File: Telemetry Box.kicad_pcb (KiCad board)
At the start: 4 copper layers, 44.6 x 36.8 mm, 82 parts, among them J1 USB_C_Receptacle, J2 DC 5V In, J3 Conn_01x06, J4 Thermistor Molex, J5 Micro_SD_Card, J6 Thermistor Molex, J8 SMA, Q1 MMBT2222A-TP, SW2 SW_Push, U1 AP2112K-1.8, U10 MAX-M10S, U2 TPS62160DSG, U3 STM32F373CCTx, U4 LSM6DSRXTR, U5 MCP6L01x-xLT, U7 BMP585, U8 MCP6L01x-xLT, U9 USBLC6-2P6, X1 32.768kHz

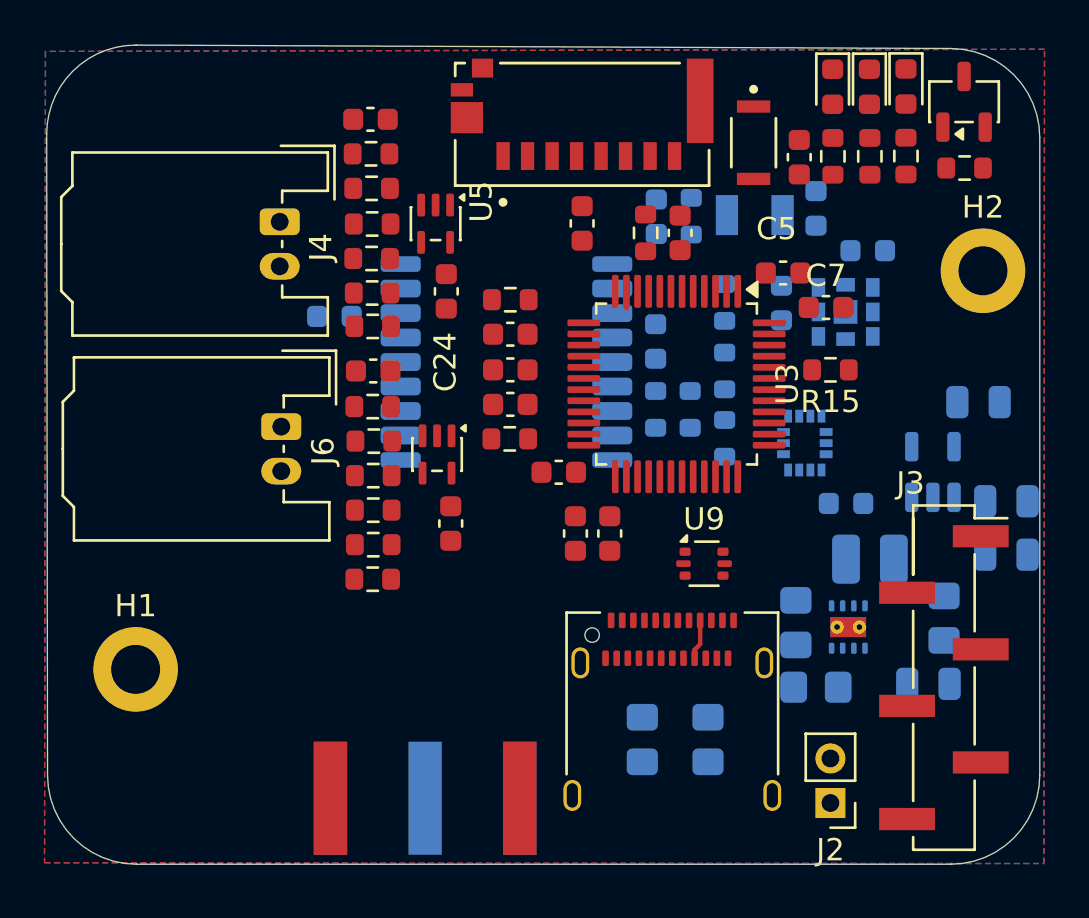
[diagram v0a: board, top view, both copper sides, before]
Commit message: Shrank board, updated all cap footprints. Updated thermistor headers to be vertical
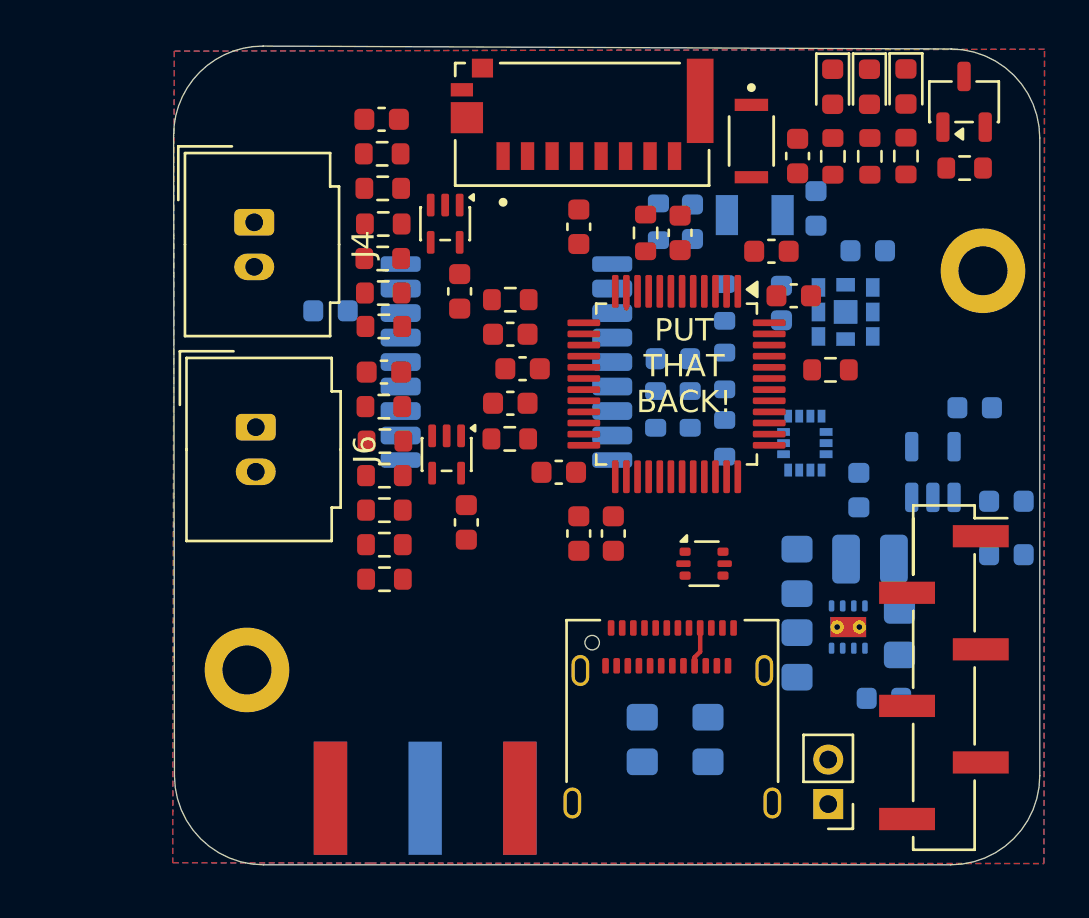
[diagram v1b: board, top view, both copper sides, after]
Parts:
- removed C11, C12, C17, C18, C20, C21, C5, C7, C9: 100nF, Capacitor_SMD:C_0603_1608Metric
- added C23: 100nF, Capacitor_SMD:C_0603_1608Metric, F.Cu at (131.7, 119.2)
- added C25: 100nF, Capacitor_SMD:C_0603_1608Metric, F.Cu at (128.3, 122.8)
- added C29: 100nF, Capacitor_SMD:C_0603_1608Metric, B.Cu at (125.9, 120.1)
- added C31: 100nF, Capacitor_SMD:C_0603_1608Metric, F.Cu at (134.0, 121.2)
- added C34: 100nF, Capacitor_SMD:C_0603_1608Metric, F.Cu at (146.7, 119.4)
- added C35: 100nF, Capacitor_SMD:C_0603_1608Metric, F.Cu at (138.6, 130.1)
- added C36: 100nF, Capacitor_SMD:C_0603_1608Metric, F.Cu at (145.7, 117.4)
- added C37: 100nF, Capacitor_SMD:C_0603_1608Metric, F.Cu at (134.5, 122.7)
- added C38: 100nF, Capacitor_SMD:C_0603_1608Metric, F.Cu at (137.1, 116.3)
- C1, C2: value 1u -> 1uF; footprint Capacitor_SMD:C_0805_2012Metric -> Capacitor_SMD:C_0603_1608Metric
- C28, C30: moved to B.Cu
- C3: value 10u -> 10uF; footprint Capacitor_SMD:C_0805_2012Metric -> Capacitor_SMD:C_0603_1608Metric
- C32, C33: moved to F.Cu
- C4: value 22u -> 22uF; footprint Capacitor_SMD:C_0805_2012Metric -> Capacitor_SMD:C_0603_1608Metric
- J4, J6: footprint Connector_Molex:Molex_MicroClasp_55935-0230_1x02_P2.00mm_Horizontal -> Connector_Molex:Molex_MicroClasp_55932-0230_1x02_P2.00mm_Vertical
- moved C33 22.0 mm to (146.9, 113.2), turned to -90 degrees
- moved C30 18.4 mm to (149.6, 128.2)
- moved C28 13.5 mm to (141.3, 122.2), turned to 0 degrees
- moved C24 10.4 mm to (132.0, 129.6)
- moved C32 7.09 mm to (134.0, 124.2), turned to 180 degrees
- moved H1 5.00 mm to (122.2, 136.2)
- moved R4 2.30 mm to (146.8, 131.8)
- moved C3 2.10 mm to (150.8, 137.5)
- moved R3 2.10 mm to (151.4, 134.6)
- moved R5 1.68 mm to (146.8, 135.6), turned to -90 degrees
- moved C16 1.64 mm to (142.2, 116.1)
- moved R9 1.50 mm to (140.6, 116.1)
- moved J4 1.15 mm to (122.5, 116.1)
- moved J6 1.15 mm to (122.5, 125.3)
- moved R31 0.53 mm to (128.3, 132.2)
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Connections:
- C28 pad 1: /MCU/THERM2 -> +3V3
- C30 pad 1: +3V3 -> +1V8
- C32 pad 1: +3V3 -> /MCU/THERM2_ADC
- C33 pad 1: +3V3 -> PGND
- C33 pad 2: PGND -> /MCU/RESET
- J4 pad 1: PGND -> /Sensors/THERM1_V-
- J4 pad 2: /Sensors/THERM1_V- -> PGND
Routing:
- added copper zone on In2.Cu, net +3V3
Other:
- board size 44.6 x 36.8 mm -> 38.9 x 36.8 mm
- board text added: "PUT THAT BACK!"

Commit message: Finished Rev2 signal routing
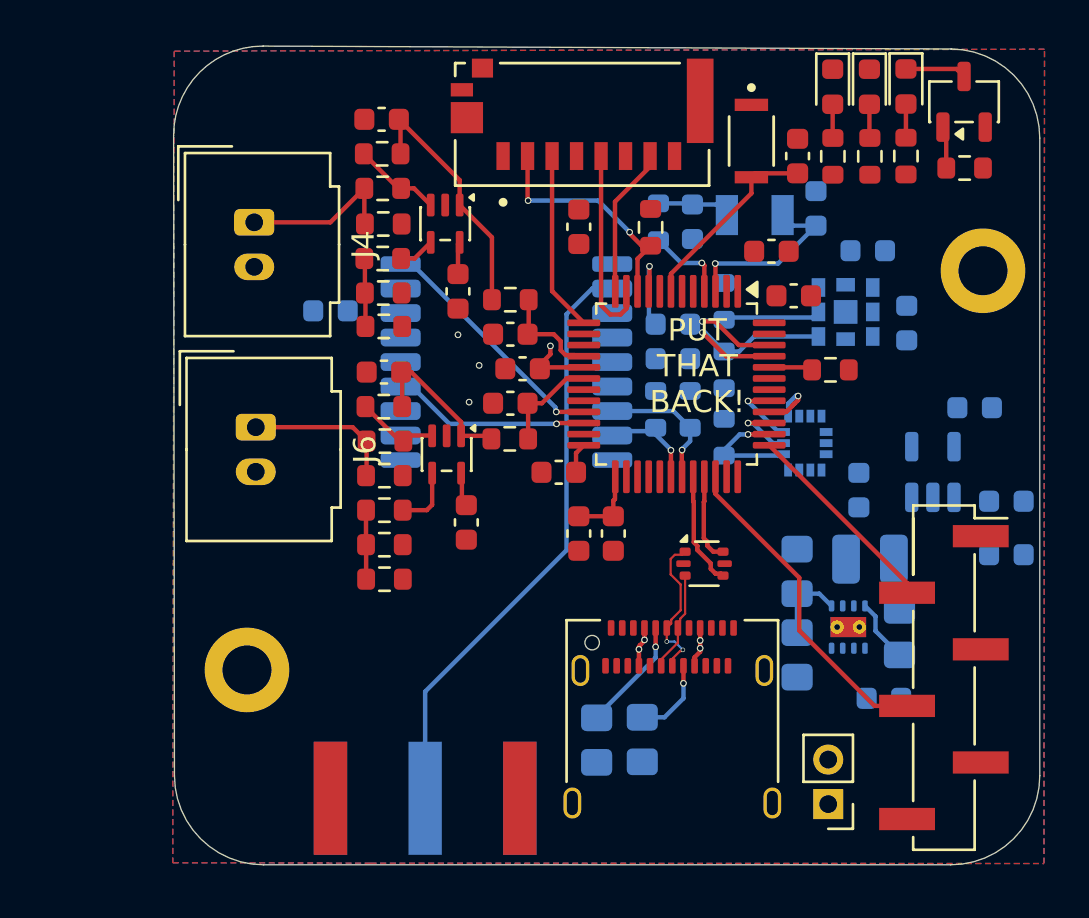
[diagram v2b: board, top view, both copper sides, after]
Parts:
- C6: moved to B.Cu
- moved C27 5.70 mm to (151.8, 120.7), turned to 90 degrees
- moved R2 5.00 mm to (137.8, 139.4)
- moved C6 4.11 mm to (141.3, 120.7), turned to 0 degrees
- moved R14 0.34 mm to (140.3, 116.3)
- moved C23 0.07 mm to (131.6, 119.2)
- moved R11 0.06 mm to (143.6, 122.8)
- moved R12 0.06 mm to (143.6, 119.7)
- moved R13 0.06 mm to (143.6, 125.8)
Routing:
- net Net-(J8-In): track 0.00 -> 26.9 mm
- net +3V3: track 0.00 -> 14.8 mm, vias 0 -> 2
- net /MCU/SWDIO: track 0.00 -> 14.7 mm
- net /MCU/THERM1: track 0.00 -> 11.4 mm
- net /MCU/GPS_RST: track 0.00 -> 11.0 mm, vias 0 -> 1
- net /MCU/SD_CS: track 0.00 -> 10.6 mm, vias 0 -> 2
- net /MCU/BMP_SCX: track 0.00 -> 9.28 mm, vias 0 -> 1
- net /MCU/SWCLK: track 0.00 -> 9.19 mm
- net /MCU/GPS_TP: track 0.00 -> 8.93 mm, vias 0 -> 1
- net /MCU/RESET: track 0.00 -> 8.77 mm
- net /MCU/BMP_SDX: track 0.30 -> 8.83 mm, vias 0 -> 1
- net /MCU/Crystal_1: track 0.00 -> 8.18 mm, vias 0 -> 1
- net /MCU/SD_CLK: track 0.77 -> 8.89 mm
- net /MCU/SD_MOSI: track 0.00 -> 8.08 mm
- net /MCU/THERM2: track 0.00 -> 7.23 mm
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
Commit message: Finished Rev2 layout
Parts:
- moved H1 4.41 mm to (121.6, 140.6)
- moved R16 0.14 mm to (128.2, 116.1)
- moved R22 0.14 mm to (128.2, 114.5)
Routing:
- net +5V: track 3.61 -> 34.4 mm, vias 4 -> 18
- net /MCU/RESET: track 8.77 -> 35.7 mm
- net +3V3: track 14.8 -> 34.3 mm, vias 2 -> 44
- net +1V8: track 0.00 -> 11.3 mm, vias 0 -> 8
- net AGND: track 0.00 -> 2.09 mm
- net PGND: vias 3 -> 20
- net (no net): vias 0 -> 1
- added copper zone on B.Cu, net +1V8
- added copper zone on In2.Cu, net +1V8
- added copper zone on B.Cu, net +3V3
- added copper zone on F.Cu, net +3V3
- added copper zone on B.Cu, net +5V
- added copper zone on F.Cu, net +5V
- added copper zone on In2.Cu, net +5V
- added copper zone on B.Cu, net /Converters/5_+3V3_SW
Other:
- board text added: "Fuad Ahmed Telemetry Board Rev2 | Sep 2026"

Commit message: Final Rev2 - Resolved all DRC
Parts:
- moved C22 0.15 mm to (128.2, 111.3)
- moved R26 0.15 mm to (128.2, 112.9)
- moved D1 0.09 mm to (150.1, 110.1)
- moved D2 0.09 mm to (148.5, 110.1)
- moved D4 0.09 mm to (151.8, 110.1)
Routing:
- net /MCU/BMP_SDX: track 8.83 -> 8.33 mm
- net +5V: vias 18 -> 17
